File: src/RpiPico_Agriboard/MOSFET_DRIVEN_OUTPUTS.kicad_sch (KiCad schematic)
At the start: 7 parts, among them J12 Conn_02x03_Odd_Even, J23 Screw_Terminal_01x02, Q5 AP3404

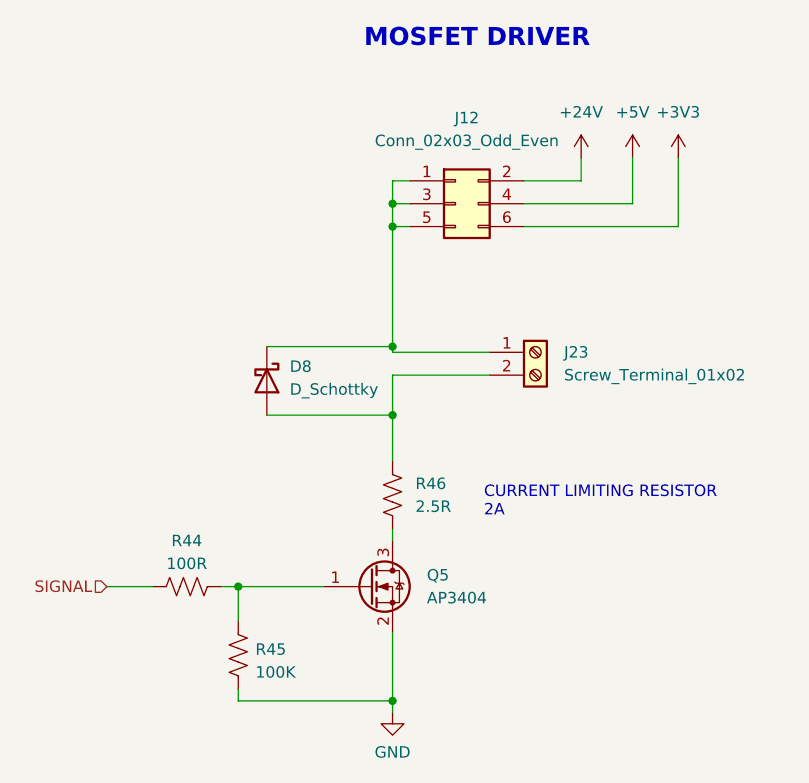
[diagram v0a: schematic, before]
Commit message: Revert "schematic updates completed"
This reverts commit 0124993096667d53f20fd59dec80d3f5a1efcd43.
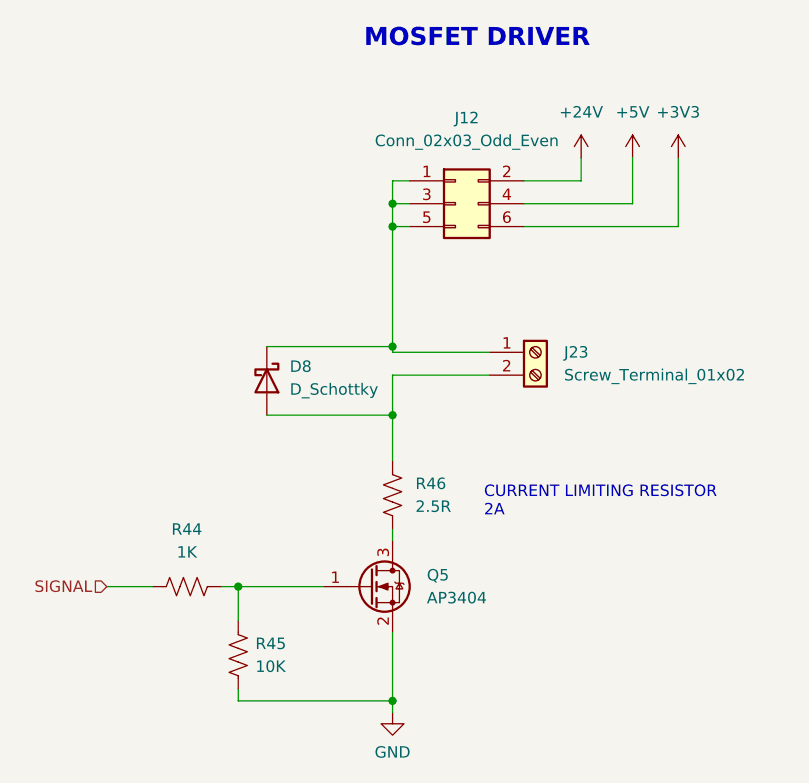
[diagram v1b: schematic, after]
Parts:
- R44: value 100R -> 1K
- R45: value 100K -> 10K
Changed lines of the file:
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@@
   (symbol (lib_id "Device:R_US") (at 106.68 87.63 90) (unit 1)
     (in_bom yes) (on_board yes) (dnp no) (fields_autoplaced)
-    (property "Reference" "R44" (at 106.68 82.55 90)
+    (property "Reference" "R44" (at 106.68 81.28 90)
       (effects (font (size 1.27 1.27)))
     )
-    (property "Value" "100R" (at 106.68 85.09 90)
+    (property "Value" "1K" (at 106.68 83.82 90)
       (effects (font (size 1.27 1.27)))
     )
@@
   (symbol (lib_id "Device:R_US") (at 112.395 95.25 0) (unit 1)
     (in_bom yes) (on_board yes) (dnp no) (fields_autoplaced)
-    (property "Reference" "R45" (at 114.3 94.615 0)
+    (property "Reference" "R45" (at 114.3 93.9799 0)
       (effects (font (size 1.27 1.27)) (justify left))
     )
-    (property "Value" "100K" (at 114.3 97.155 0)
+    (property "Value" "10K" (at 114.3 96.5199 0)
       (effects (font (size 1.27 1.27)) (justify left))
     )
